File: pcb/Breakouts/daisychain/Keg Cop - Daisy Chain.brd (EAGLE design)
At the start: 33.2 x 43.2 mm, 3 parts

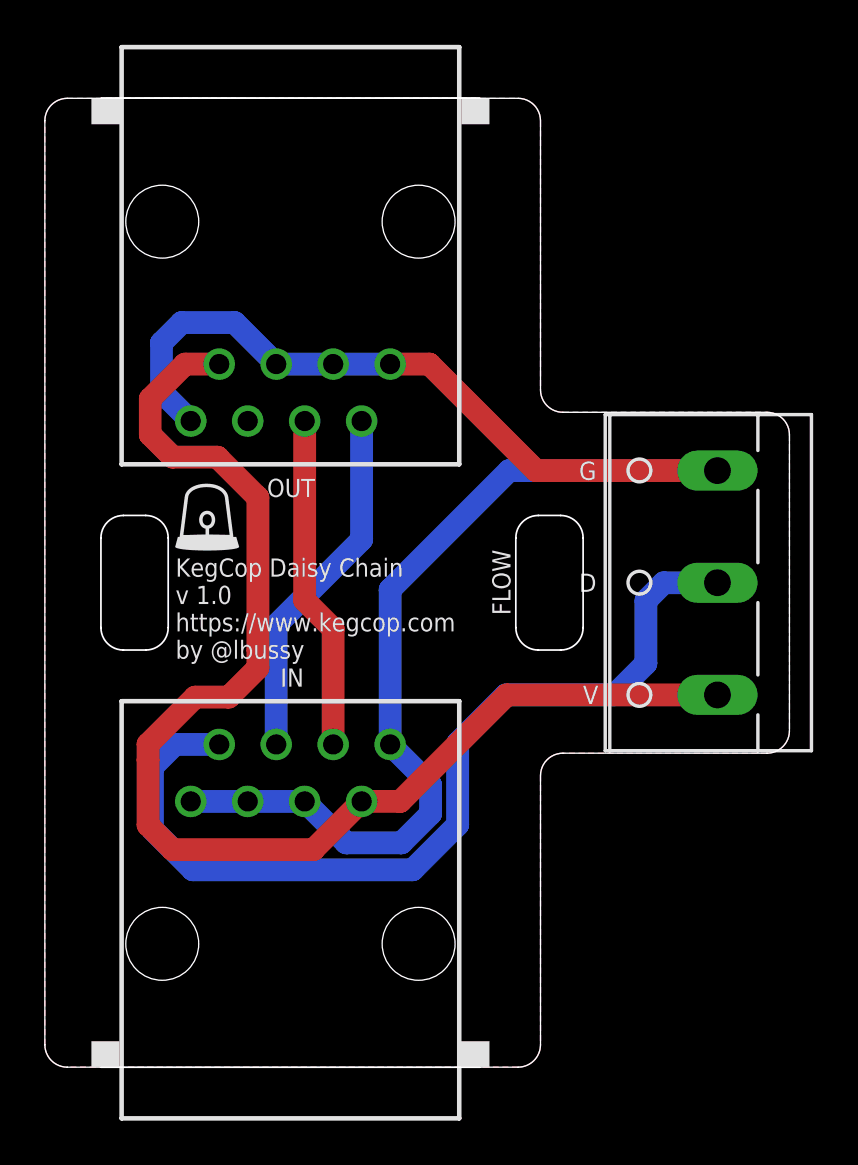
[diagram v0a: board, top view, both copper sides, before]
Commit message: Add series resistor
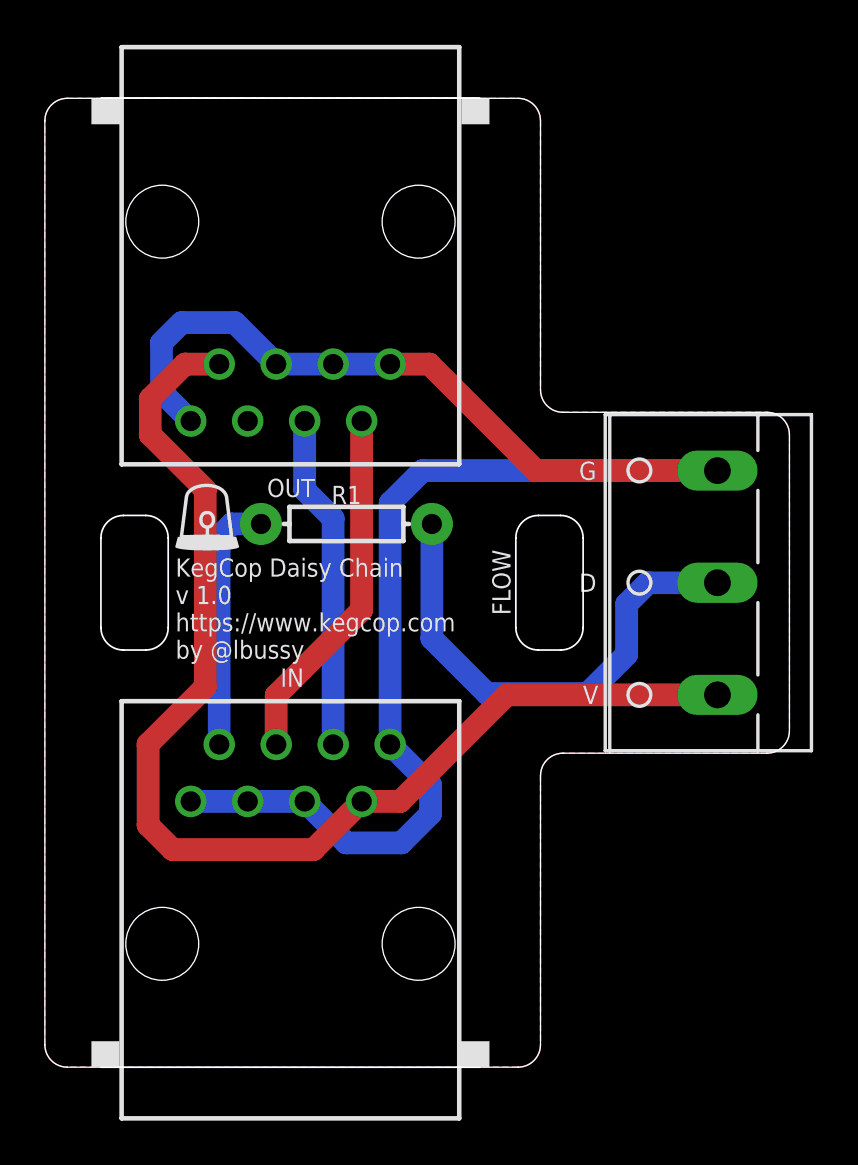
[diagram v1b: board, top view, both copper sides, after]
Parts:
- added R1: 1k, SparkFun-Resistors:AXIAL-0.3
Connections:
- new net N$1: FLOW.2, R1.P$2
- net DATA0: now also R1.P$1; no longer FLOW.2
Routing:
- net DATA0: track 41.2 -> 11.4 mm
- net N$1: track 0.00 -> 22.2 mm
- net 5VD: track 57.5 -> 53.5 mm
- net GND: track 71.5 -> 73.7 mm
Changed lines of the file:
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@@
 <attribute name="VALUE" x="33.6476" y="16.2952" size="1.27" layer="27" ratio="10" rot="R90"/>
+</element>
+<element name="R1" library="SparkFun-Resistors" library_urn="urn:adsk.eagle:library:532" package="AXIAL-0.3" package3d_urn="urn:adsk.eagle:package:39658/1" value="1k" x="13.446759375" y="24.2214375" smashed="yes">
+<attribute name="NAME" x="13.446759375" y="25.1104375" size="0.8128" layer="25" font="vector" align="bottom-center"/>
+<attribute name="PROD_ID" value="RES-08380" x="13.446759375" y="24.2214375" size="1.778" layer="27" display="off"/>
 </element>
 </elements>
@@
 <wire x1="21.9" y1="26.6" x2="29.99" y2="26.6" width="1.016" layer="1"/>
 <wire x1="17.15" y1="31.35" x2="21.9" y2="26.6" width="1.016" layer="1"/>
-<wire x1="15.395" y1="14.39" x2="15.395" y2="21.295" width="1.016" layer="16"/>
-<wire x1="20.7" y1="26.6" x2="29.99" y2="26.6" width="1.016" layer="16"/>
-<wire x1="15.395" y1="21.295" x2="20.7" y2="26.6" width="1.016" layer="16"/>
+<wire x1="16.8392" y1="26.6" x2="29.99" y2="26.6" width="1.016" layer="16"/>
+<wire x1="15.395" y1="25.1558" x2="16.8392" y2="26.6" width="1.016" layer="16"/>
+<wire x1="15.395" y1="14.39" x2="15.395" y2="25.1558" width="1.016" layer="16"/>
 </signal>
 <signal name="DATA0">
 <contactref element="IN" pad="2"/>
-<contactref element="FLOW" pad="2"/>
-<wire x1="7.775" y1="14.39" x2="5.79" y2="14.39" width="1.016" layer="16"/>
-<wire x1="5.79" y1="14.39" x2="4.8" y2="13.4" width="1.016" layer="16"/>
-<wire x1="4.8" y1="13.4" x2="4.8" y2="10.6" width="1.016" layer="16"/>
-<wire x1="16.4" y1="8.8" x2="18.4078" y2="10.8078" width="1.016" layer="16"/>
-<wire x1="26.8" y1="20.8" x2="27.6" y2="21.6" width="1.016" layer="16"/>
-<wire x1="27.6" y1="21.6" x2="29.99" y2="21.6" width="1.016" layer="16"/>
-<wire x1="4.8" y1="10.6" x2="6.6" y2="8.8" width="1.016" layer="16"/>
-<wire x1="18.4078" y1="10.8078" x2="18.4078" y2="14.45240625" width="1.016" layer="16"/>
-<wire x1="18.4078" y1="14.45240625" x2="20.55539375" y2="16.6" width="1.016" layer="16"/>
-<wire x1="20.55539375" y1="16.6" x2="25.4" y2="16.6" width="1.016" layer="16"/>
-<wire x1="26.8" y1="18" x2="26.8" y2="20.8" width="1.016" layer="16"/>
-<wire x1="25.4" y1="16.6" x2="26.8" y2="18" width="1.016" layer="16"/>
-<wire x1="6.6" y1="8.8" x2="16.4" y2="8.8" width="1.016" layer="16"/>
+<contactref element="R1" pad="P$1"/>
+<wire x1="7.775" y1="14.39" x2="7.775" y2="23.6652375" width="1.016" layer="16"/>
+<wire x1="8.3312" y1="24.2214375" x2="9.636759375" y2="24.2214375" width="1.016" layer="16"/>
+<wire x1="7.775" y1="23.6652375" x2="8.3312" y2="24.2214375" width="1.016" layer="16"/>
 </signal>
 <signal name="5VD">
@@
 <wire x1="7.775" y1="31.35" x2="6.25" y2="31.35" width="1.016" layer="1"/>
 <wire x1="6.25" y1="31.35" x2="4.7" y2="29.8" width="1.016" layer="1"/>
-<wire x1="4.6" y1="10.8" x2="4.6" y2="13.7" width="1.016" layer="1"/>
+<wire x1="4.6" y1="10.8" x2="4.6" y2="14.4" width="1.016" layer="1"/>
 <wire x1="4.7" y1="28.2" x2="4.7" y2="29.8" width="1.016" layer="1"/>
 <wire x1="5.7" y1="9.7" x2="11.975" y2="9.7" width="1.016" layer="1"/>
 <wire x1="4.6" y1="10.8" x2="5.7" y2="9.7" width="1.016" layer="1"/>
 <wire x1="14.125" y1="11.85" x2="15.85" y2="11.85" width="1.016" layer="1"/>
-<wire x1="7.7" y1="27.2" x2="5.7" y2="27.2" width="1.016" layer="1"/>
-<wire x1="5.7" y1="27.2" x2="4.7" y2="28.2" width="1.016" layer="1"/>
-<wire x1="9.5" y1="18.6" x2="9.5" y2="25.4" width="1.016" layer="1"/>
-<wire x1="9.5" y1="25.4" x2="7.7" y2="27.2" width="1.016" layer="1"/>
-<wire x1="4.6" y1="13.7" x2="4.6" y2="14.4" width="1.016" layer="1"/>
-<wire x1="6.7" y1="16.5" x2="8.2" y2="16.5" width="1.016" layer="1"/>
-<wire x1="8.2" y1="16.5" x2="9.5" y2="17.8" width="1.016" layer="1"/>
-<wire x1="9.5" y1="17.8" x2="9.5" y2="18.6" width="1.016" layer="1"/>
-<wire x1="4.6" y1="14.4" x2="6.7" y2="16.5" width="1.016" layer="1"/>
+<wire x1="7.153040625" y1="25.746959375" x2="4.7" y2="28.2" width="1.016" layer="1"/>
+<wire x1="4.6" y1="14.4" x2="7.153040625" y2="16.953040625" width="1.016" layer="1"/>
+<wire x1="7.153040625" y1="16.953040625" x2="7.153040625" y2="25.746959375" width="1.016" layer="1"/>
 </signal>
 <signal name="DATA1">
 <contactref element="IN" pad="4"/>
 <contactref element="OUT" pad="2"/>
-<wire x1="10.315" y1="14.39" x2="10.315" y2="19.715" width="1.016" layer="16"/>
-<wire x1="14.125" y1="23.525" x2="14.125" y2="28.81" width="1.016" layer="16"/>
-<wire x1="10.315" y1="19.715" x2="14.125" y2="23.525" width="1.016" layer="16"/>
+<wire x1="10.315" y1="14.39" x2="10.315" y2="16.578640625" width="1.016" layer="1"/>
+<wire x1="14.125" y1="20.388640625" x2="14.125" y2="28.81" width="1.016" layer="1"/>
+<wire x1="10.315" y1="16.578640625" x2="14.125" y2="20.388640625" width="1.016" layer="1"/>
 </signal>
 <signal name="DATA2">
 <contactref element="IN" pad="6"/>
 <contactref element="OUT" pad="4"/>
-<wire x1="12.855" y1="14.39" x2="12.855" y2="19.545" width="1.016" layer="1"/>
-<wire x1="11.585" y1="20.815" x2="11.585" y2="28.81" width="1.016" layer="1"/>
-<wire x1="12.855" y1="19.545" x2="11.585" y2="20.815" width="1.016" layer="1"/>
+<wire x1="12.855" y1="14.39" x2="12.855" y2="24.467759375" width="1.016" layer="16"/>
+<wire x1="11.585" y1="25.737759375" x2="11.585" y2="28.81" width="1.016" layer="16"/>
+<wire x1="12.855" y1="24.467759375" x2="11.585" y2="25.737759375" width="1.016" layer="16"/>
+</signal>
+<signal name="N$1">
+<contactref element="FLOW" pad="2"/>
+<contactref element="R1" pad="P$2"/>
+<wire x1="17.256759375" y1="24.2214375" x2="17.256759375" y2="19.110959375" width="1.016" layer="16"/>
+<wire x1="19.715478125" y1="16.652240625" x2="24.190959375" y2="16.652240625" width="1.016" layer="16"/>
+<wire x1="24.190959375" y1="16.652240625" x2="25.943559375" y2="18.404840625" width="1.016" layer="16"/>
+<wire x1="26.893359375" y1="21.6" x2="29.99" y2="21.6" width="1.016" layer="16"/>
+<wire x1="17.256759375" y1="19.110959375" x2="19.715478125" y2="16.652240625" width="1.016" layer="16"/>
+<wire x1="25.943559375" y1="18.404840625" x2="25.943559375" y2="20.6502" width="1.016" layer="16"/>
+<wire x1="25.943559375" y1="20.6502" x2="26.893359375" y2="21.6" width="1.016" layer="16"/>
 </signal>
 </signals>

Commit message: Updated Daisy Chain
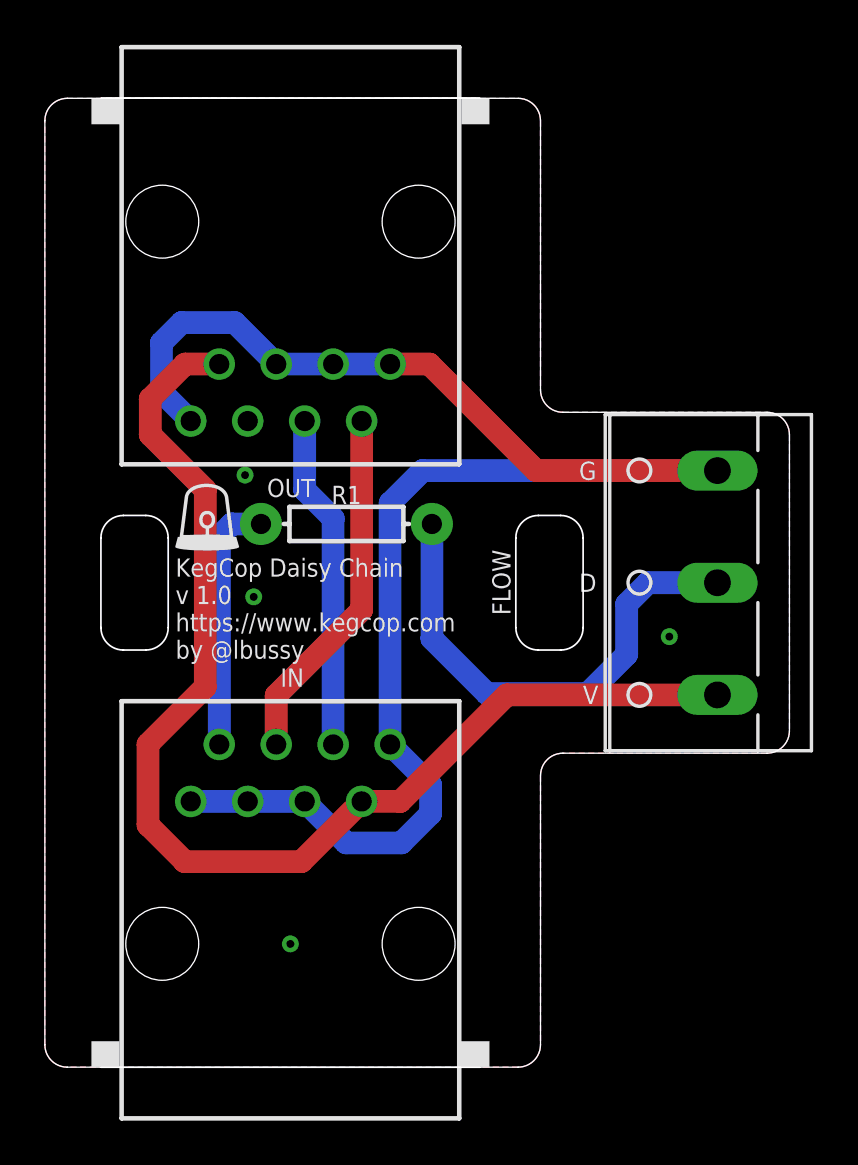
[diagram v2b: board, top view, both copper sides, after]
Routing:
- net GND: vias 0 -> 4
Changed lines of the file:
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@@
 <text x="24.110578125" y="21.6" size="0.8128" layer="26" rot="MR0" align="center-right">D</text>
 <text x="24.110578125" y="16.6" size="0.8128" layer="26" rot="MR0" align="center-right">V</text>
-<text x="12.3" y="21.6" size="0.8128" layer="26" rot="MR0" align="center">Components
+<text x="12.59971875" y="20.4925625" size="0.8128" layer="26" rot="MR0" align="center">Components
 other
 side</text>
@@
 </class>
 </classes>
-<designrules name="default">
+<designrules name="default *">
 <description language="de">&lt;b&gt;EAGLE Design Rules&lt;/b&gt;
 &lt;p&gt;
@@
 <param name="mlMinCreamFrame" value="0mil"/>
 <param name="mlMaxCreamFrame" value="0mil"/>
-<param name="mlViaStopLimit" value="0mil"/>
+<param name="mlViaStopLimit" value="30mil"/>
 <param name="srRoundness" value="0"/>
 <param name="srMinRoundness" value="0mil"/>
@@
 <wire x1="15.395" y1="25.1558" x2="16.8392" y2="26.6" width="1.016" layer="16"/>
 <wire x1="15.395" y1="14.39" x2="15.395" y2="25.1558" width="1.016" layer="16"/>
+<via x="10.9474" y="5.496559375" extent="1-16" drill="0.35"/>
+<via x="8.925559375" y="26.400759375" extent="1-16" drill="0.35"/>
+<via x="9.311640625" y="20.970240625" extent="1-16" drill="0.35"/>
+<via x="27.84348125" y="19.19731875" extent="1-16" drill="0.35"/>
 </signal>
 <signal name="DATA0">
@@
 <wire x1="20.6" y1="16.6" x2="29.99" y2="16.6" width="1.016" layer="1"/>
 <wire x1="15.85" y1="11.85" x2="20.6" y2="16.6" width="1.016" layer="1"/>
-<wire x1="14.125" y1="11.85" x2="11.975" y2="9.7" width="1.016" layer="1"/>
+<wire x1="14.125" y1="11.85" x2="11.441596875" y2="9.166596875" width="1.016" layer="1"/>
 <wire x1="7.775" y1="31.35" x2="6.25" y2="31.35" width="1.016" layer="1"/>
 <wire x1="6.25" y1="31.35" x2="4.7" y2="29.8" width="1.016" layer="1"/>
 <wire x1="4.6" y1="10.8" x2="4.6" y2="14.4" width="1.016" layer="1"/>
 <wire x1="4.7" y1="28.2" x2="4.7" y2="29.8" width="1.016" layer="1"/>
-<wire x1="5.7" y1="9.7" x2="11.975" y2="9.7" width="1.016" layer="1"/>
-<wire x1="4.6" y1="10.8" x2="5.7" y2="9.7" width="1.016" layer="1"/>
+<wire x1="6.233403125" y1="9.166596875" x2="11.441596875" y2="9.166596875" width="1.016" layer="1"/>
+<wire x1="4.6" y1="10.8" x2="6.233403125" y2="9.166596875" width="1.016" layer="1"/>
 <wire x1="14.125" y1="11.85" x2="15.85" y2="11.85" width="1.016" layer="1"/>
 <wire x1="7.153040625" y1="25.746959375" x2="4.7" y2="28.2" width="1.016" layer="1"/>
